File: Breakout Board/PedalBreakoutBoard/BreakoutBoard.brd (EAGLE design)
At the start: 69.5 x 63.5 mm, 36 parts

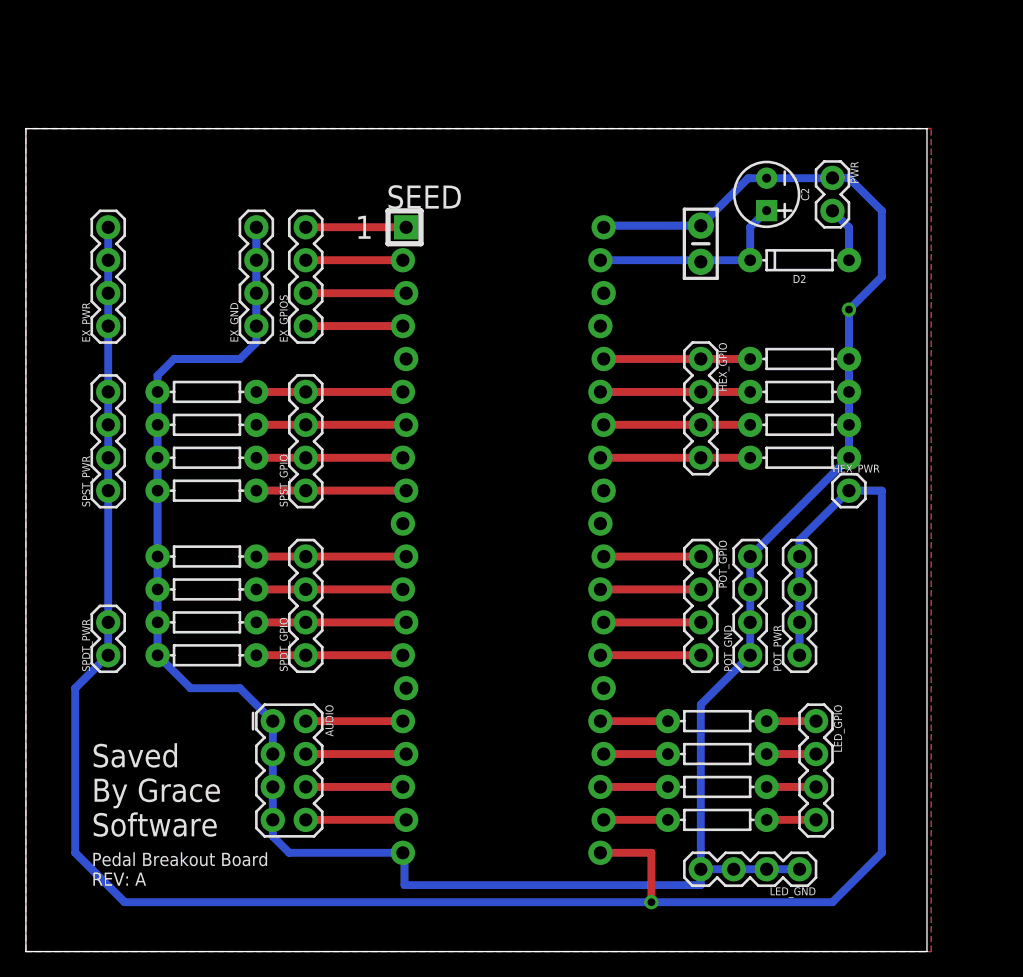
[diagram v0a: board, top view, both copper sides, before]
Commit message: DP-16 - Add mounting holes
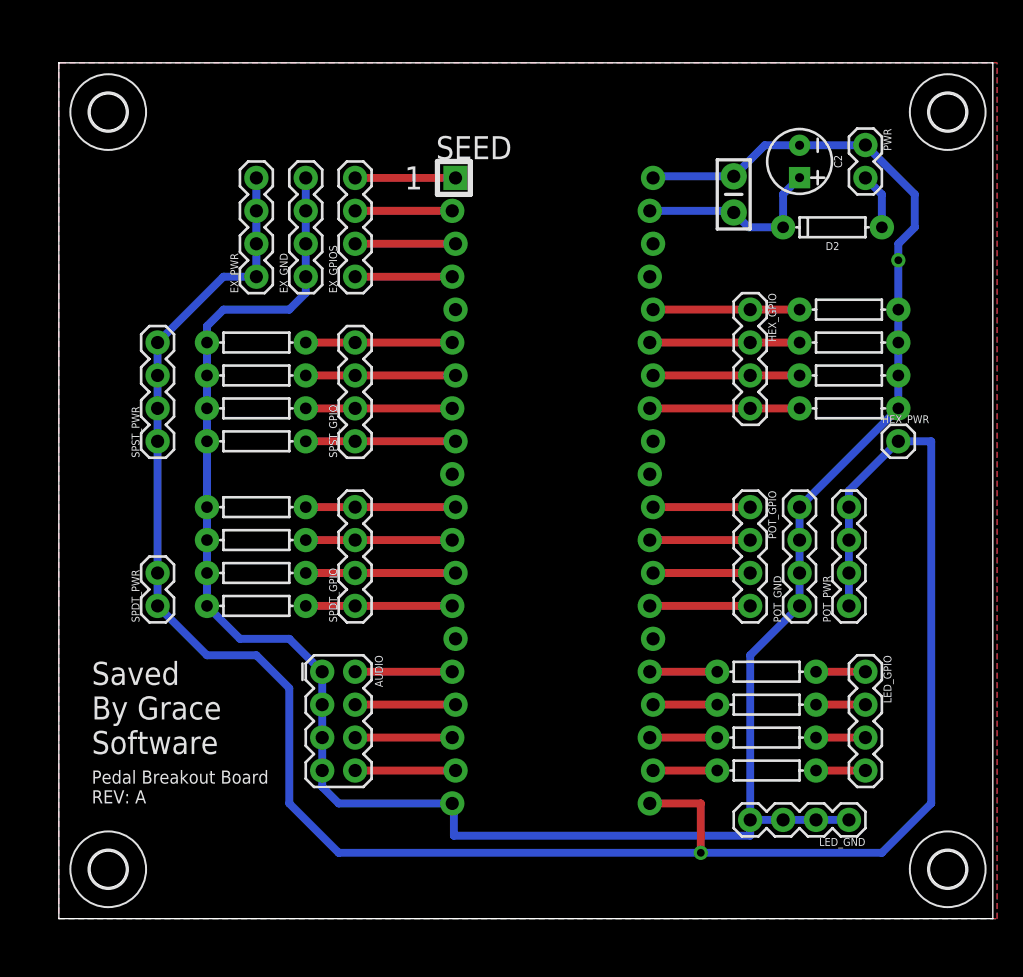
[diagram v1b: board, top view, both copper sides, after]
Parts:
- added H5, H6, H7, H8: MOUNT-HOLE2.8, holes:2,8
- moved EX_PWR 12.0 mm to (15.2, 49.5)
- moved H1 5.39 mm to (61.0, 47.0)
- moved H2 5.39 mm to (61.0, 44.5)
- moved HEX_GPIO 5.39 mm to (53.3, 47.0)
- moved L2 5.39 mm to (54.6, 16.5)
- moved SEED 5.39 mm to (38.1, 33.0)
- moved D12 5.39 mm to (15.2, 29.2)
- moved D21 5.39 mm to (15.2, 26.7)
- moved EX_GND 5.39 mm to (19.1, 49.5)
- moved EX_GPIOS 5.39 mm to (22.9, 49.5)
- moved L1 5.39 mm to (54.6, 19.1)
- moved L3 5.39 mm to (54.6, 14.0)
- moved L4 5.39 mm to (54.6, 11.4)
- moved LED_GND 5.39 mm to (61.0, 7.62)
- moved POT_GPIO 5.39 mm to (53.3, 31.8)
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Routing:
- net GND: track 184.5 -> 180.2 mm
- net +3V3_A: track 167.2 -> 164.5 mm
- net +9V_IN: track 16.0 -> 15.2 mm
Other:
- board size 69.5 x 63.5 mm -> 72.1 x 66 mm

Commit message: DP-16 - Move Daisy to edge
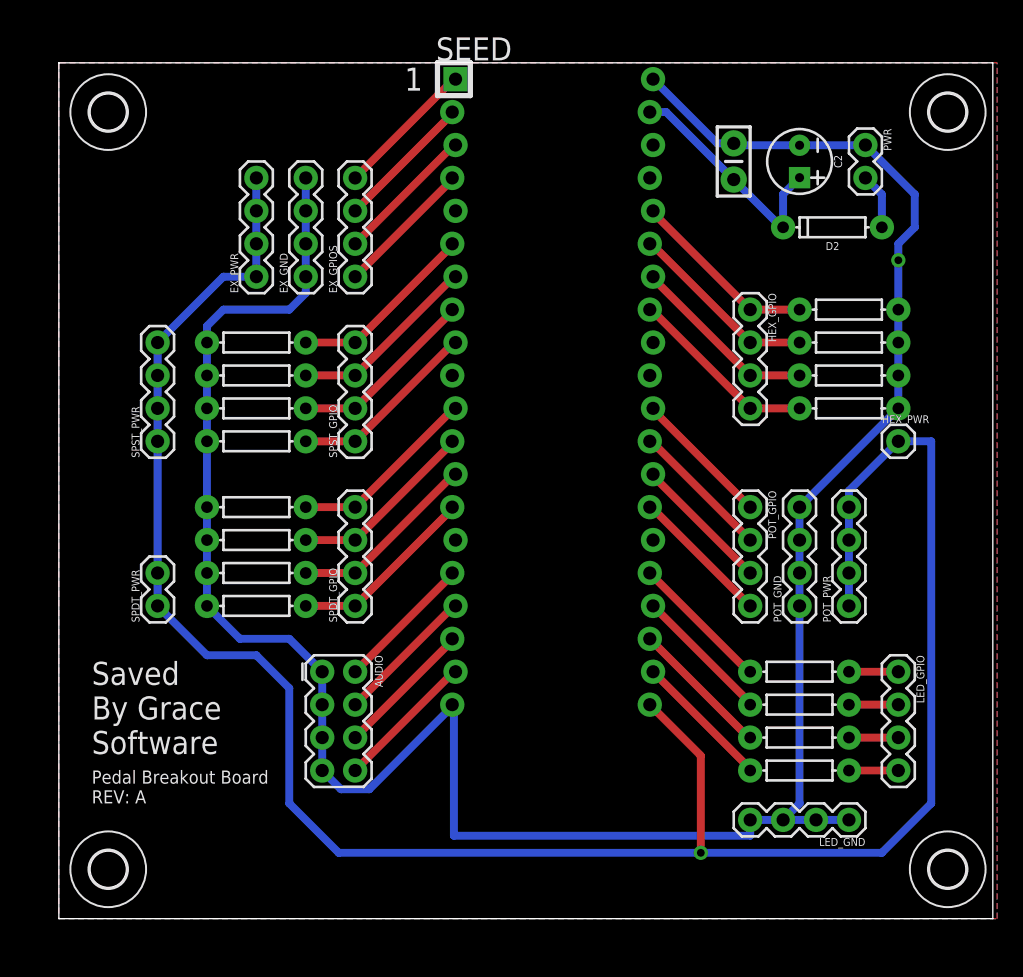
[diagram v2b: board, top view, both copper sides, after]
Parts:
- moved SEED 7.62 mm to (38.1, 40.6)
- moved C1 2.54 mm to (52.1, 58.4)
- moved L1 2.54 mm to (57.1, 19.1)
- moved L2 2.54 mm to (57.1, 16.5)
- moved L3 2.54 mm to (57.1, 14.0)
- moved L4 2.54 mm to (57.1, 11.4)
- moved LED_GPIO 2.54 mm to (64.8, 19.1)
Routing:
- net GND: track 180.2 -> 189.4 mm
- net LED4: track 4.95 -> 10.7 mm
- net LED2: track 4.95 -> 10.7 mm
- net LED1: track 5.21 -> 10.9 mm
- net LED3: track 5.21 -> 10.9 mm
- net +3V3_A: track 164.5 -> 169.8 mm
- net SPST3: track 11.3 -> 14.5 mm
- net HEX_3: track 11.3 -> 14.5 mm
- net SPDT2_2: track 11.3 -> 14.5 mm
- net IN_L: track 7.49 -> 10.7 mm
- net OUT_L: track 7.49 -> 10.7 mm
- net SPST1: track 11.3 -> 14.5 mm
- net SPDT1_2: track 11.3 -> 14.5 mm
- net POT3: track 7.49 -> 10.7 mm
- net POT1: track 7.49 -> 10.7 mm
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
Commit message: DP-16 - Shrink board
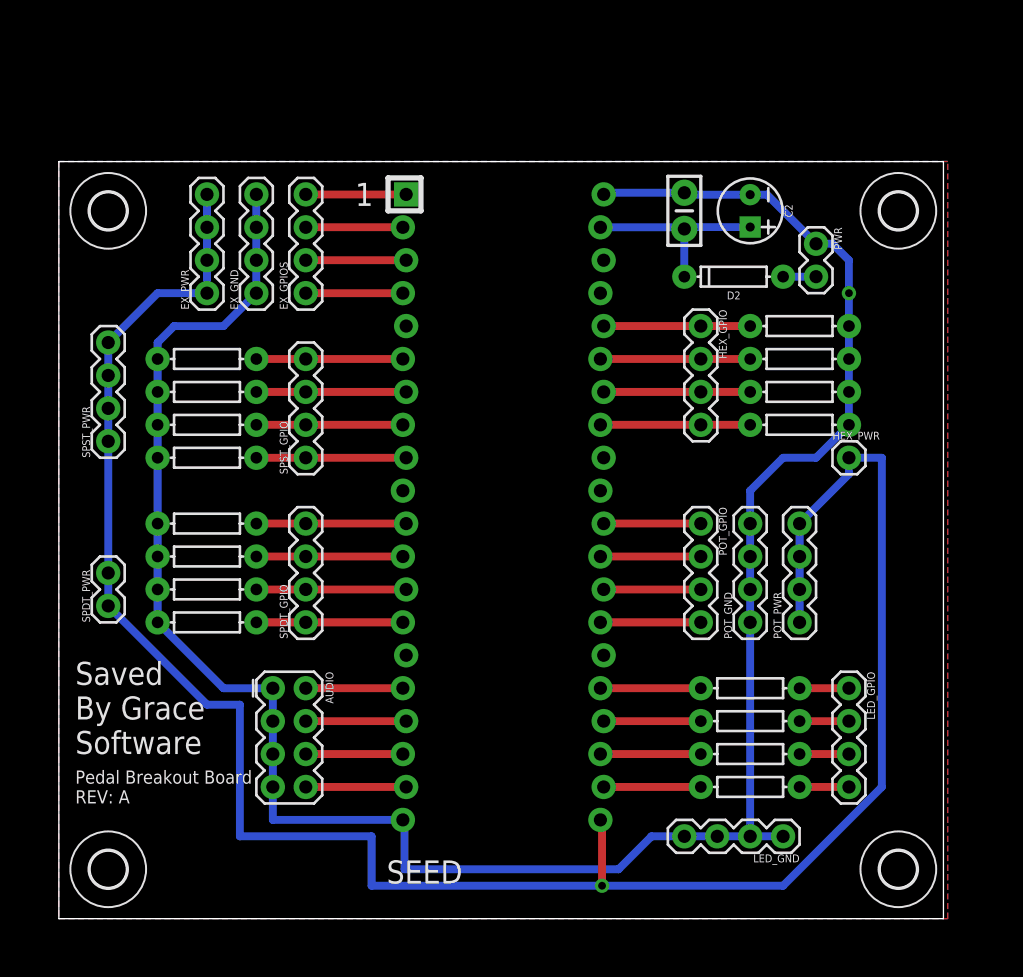
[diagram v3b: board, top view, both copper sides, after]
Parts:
- moved SEED 9.67 mm to (34.3, 31.8)
- moved D2 8.52 mm to (52.1, 49.5)
- moved H8 8.52 mm to (64.8, 54.6)
- moved PWR 8.52 mm to (58.4, 52.1)
- moved H6 7.62 mm to (3.81, 54.6)
- moved C1 5.39 mm to (48.3, 54.6)
- moved C2 5.39 mm to (53.3, 54.6)
- moved LED_GND 5.24 mm to (55.9, 6.35)
- moved H1 4.02 mm to (57.1, 45.7)
- moved H2 4.02 mm to (57.1, 43.2)
- moved HEX_GPIO 4.02 mm to (49.5, 45.7)
- moved D21 4.02 mm to (11.4, 25.4)
- moved EX_GND 4.02 mm to (15.2, 48.3)
- moved EX_PWR 4.02 mm to (11.4, 48.3)
- moved POT_GPIO 4.02 mm to (49.5, 30.5)
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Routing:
- net GND: track 189.4 -> 173.9 mm
- net +3V3_A: track 169.8 -> 164.5 mm
- net SPST3: track 14.5 -> 11.3 mm
- net IN_L: track 10.7 -> 7.49 mm
- net SPDT2_2: track 14.5 -> 11.3 mm
- net OUT_L: track 10.7 -> 7.49 mm
- net LED4: track 10.7 -> 7.49 mm
- net GPIO4: track 10.7 -> 7.49 mm
- net GPIO2: track 10.7 -> 7.49 mm
- net SPST1: track 14.5 -> 11.3 mm
- net SPDT1_2: track 14.5 -> 11.3 mm
- net POT3: track 10.7 -> 7.49 mm
- net POT1: track 10.7 -> 7.49 mm
- net LED2: track 10.7 -> 7.49 mm
- net HEX_3: track 14.5 -> 11.3 mm
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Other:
- board size 72.1 x 66 mm -> 68.2 x 58.4 mm
